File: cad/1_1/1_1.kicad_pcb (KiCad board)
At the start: 2 copper layers, 80 x 50 mm, 14 parts, among them J1 Conn_01x04_Pin, U1 ATtiny1616-M

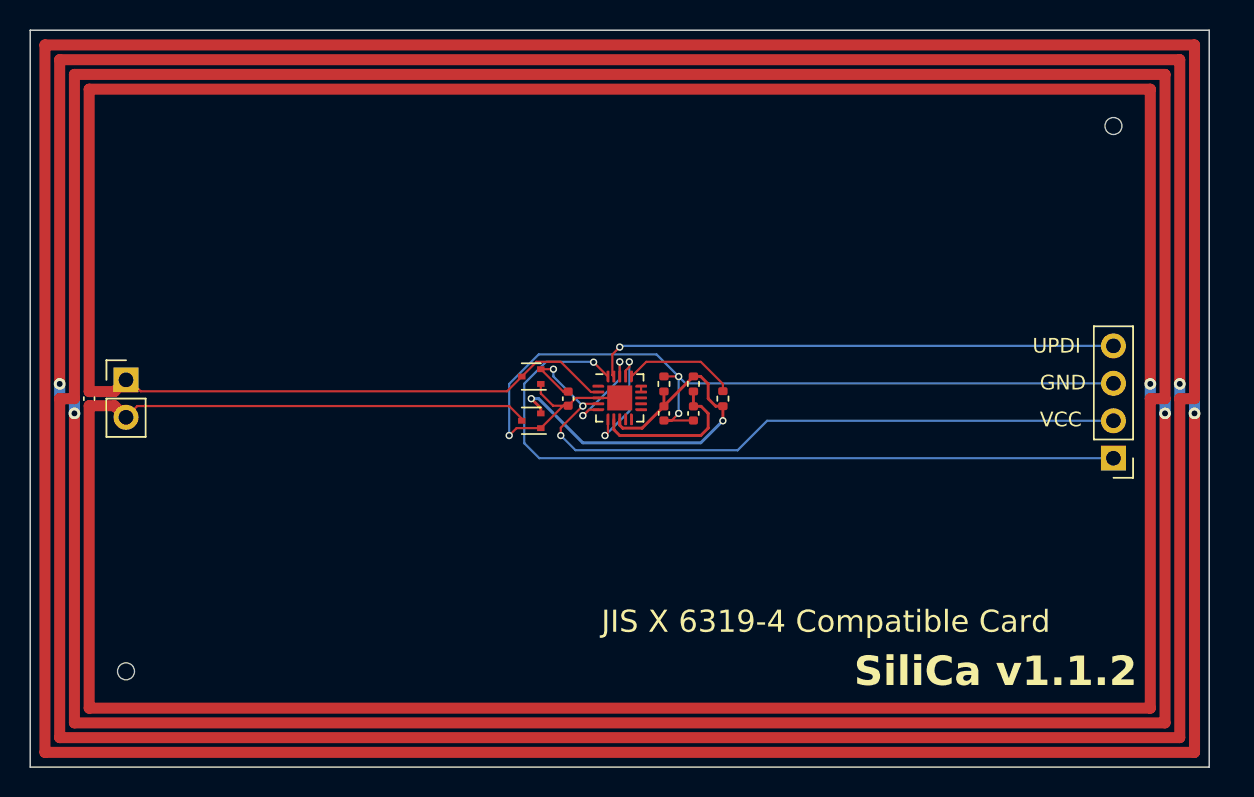
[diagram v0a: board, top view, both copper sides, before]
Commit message: 全体的に部品を左上に移動した TxDとRxDを接続した
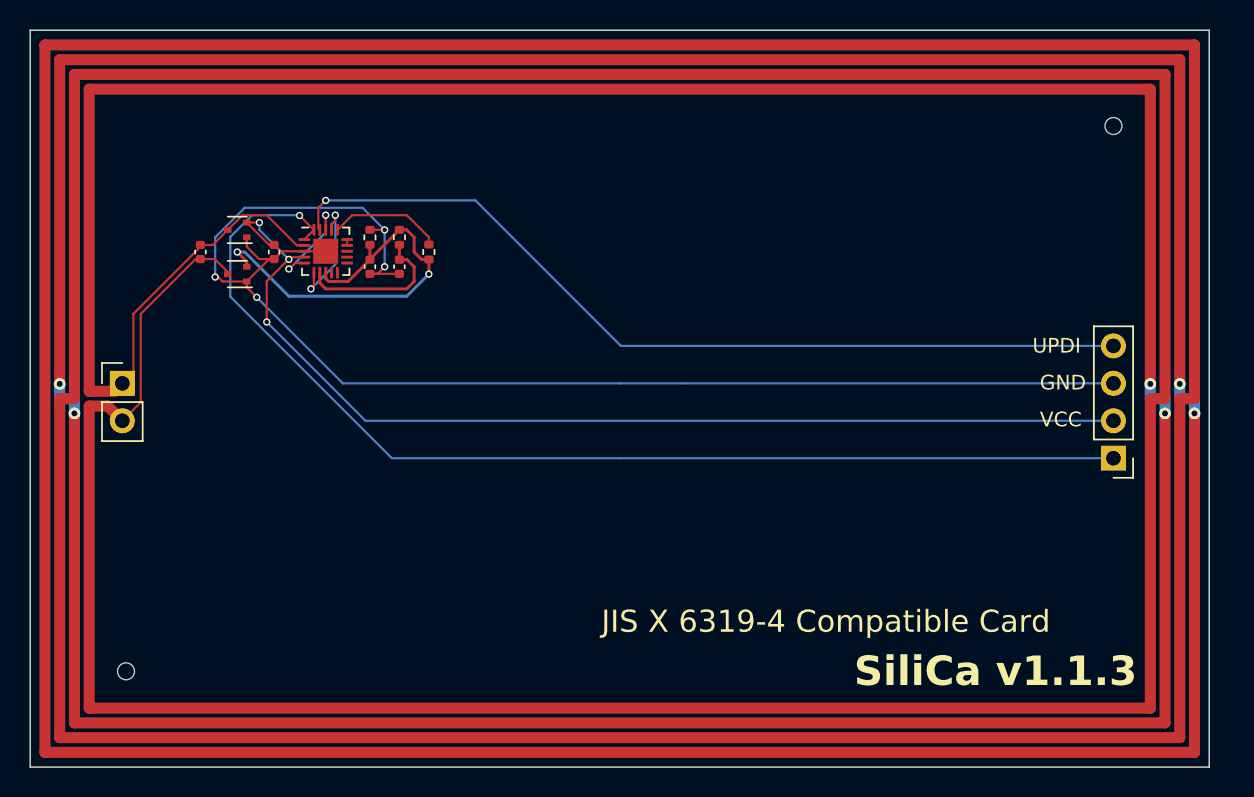
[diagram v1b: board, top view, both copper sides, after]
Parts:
- moved C2 22.3 mm to (66.5, 65.0)
- moved C3 22.3 mm to (73.0, 66.0)
- moved C4 22.3 mm to (75.0, 66.0)
- moved D1 22.3 mm to (64.0, 63.5)
- moved D2 22.3 mm to (64.0, 66.5)
- moved R1 22.3 mm to (73.0, 64.0)
- moved R2 22.3 mm to (75.0, 64.0)
- moved R3 22.3 mm to (77.0, 65.0)
- moved U1 22.3 mm to (70.0, 65.0)
- moved C1 12.5 mm to (61.5, 65.0)
- moved AE1 0.34 mm to (56.2, 74.0)
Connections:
- J1 pad 1: TxD -> RxD
- U1 pad 20: TxD -> RxD
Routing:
- net RxD: track 0.00 -> 76.1 mm, vias 0 -> 1
- net TxD: track 51.1 -> 0.00 mm, vias 1 -> 0
- net GND: track 64.2 -> 95.6 mm, vias 3 -> 4
- net EXTCLK: track 1032.4 -> 1006.2 mm
- net UPDI: track 35.7 -> 59.8 mm
- net VCC: track 49.2 -> 72.9 mm
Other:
- board text added: "SiliCa v1.1.3"
- board text removed: "SiliCa v1.1.2"

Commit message: Update component positions and configuration in PCB design files
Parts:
- moved AE1 0.25 mm to (56.5, 74.0)
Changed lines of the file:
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@@
 	(footprint "Connector_PinHeader_2.54mm:PinHeader_1x02_P2.54mm_Vertical"
 		(layer "F.Cu")
-		(at 56.25 73.96)
+		(at 56.5 73.96)
 		(descr "Through hole straight pin header, 1x02, 2.54mm pitch, single row")
 		(tags "Through hole pin header THT 1x02 2.54mm single row")
